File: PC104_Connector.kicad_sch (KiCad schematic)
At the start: 2 parts

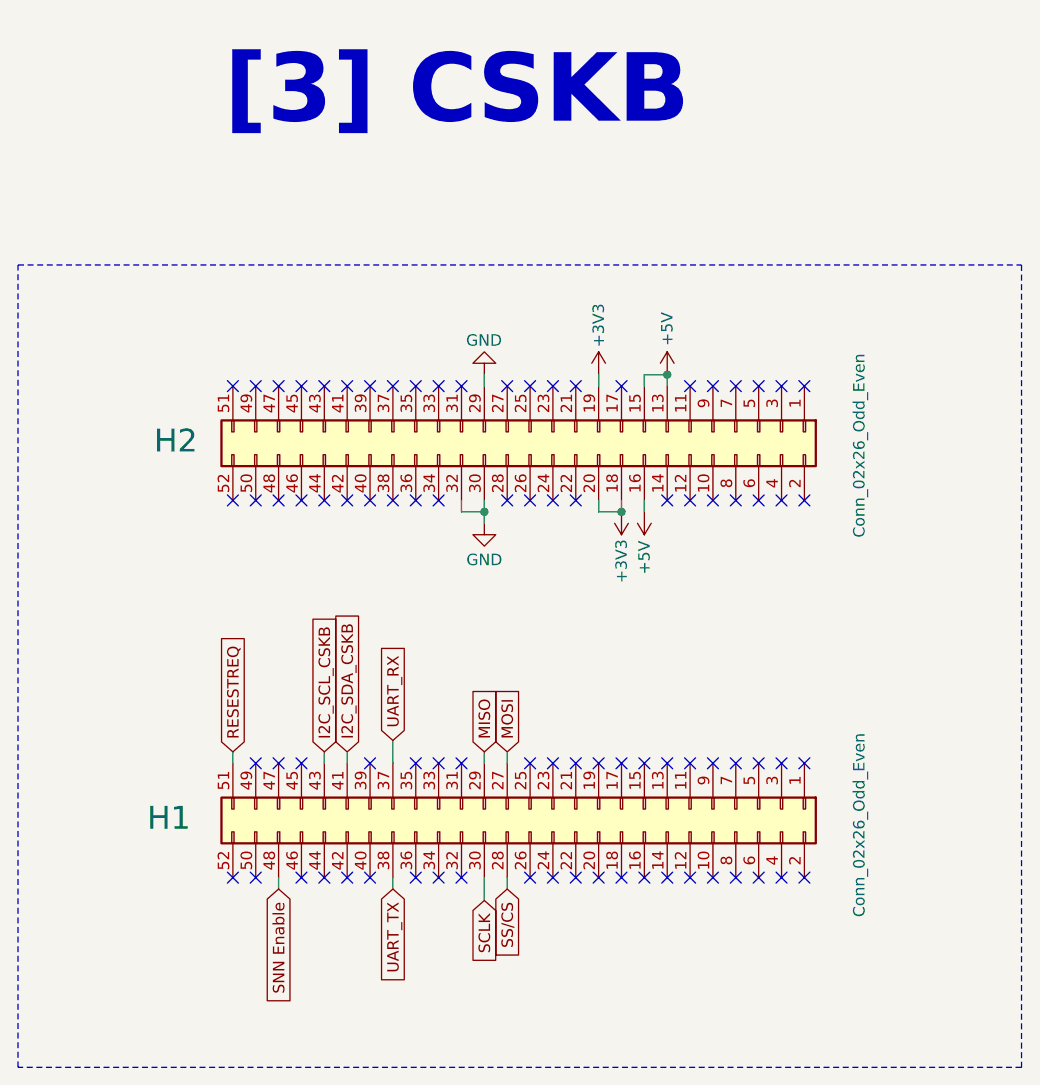
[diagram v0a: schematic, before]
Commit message: BOM update
completed the BOM list
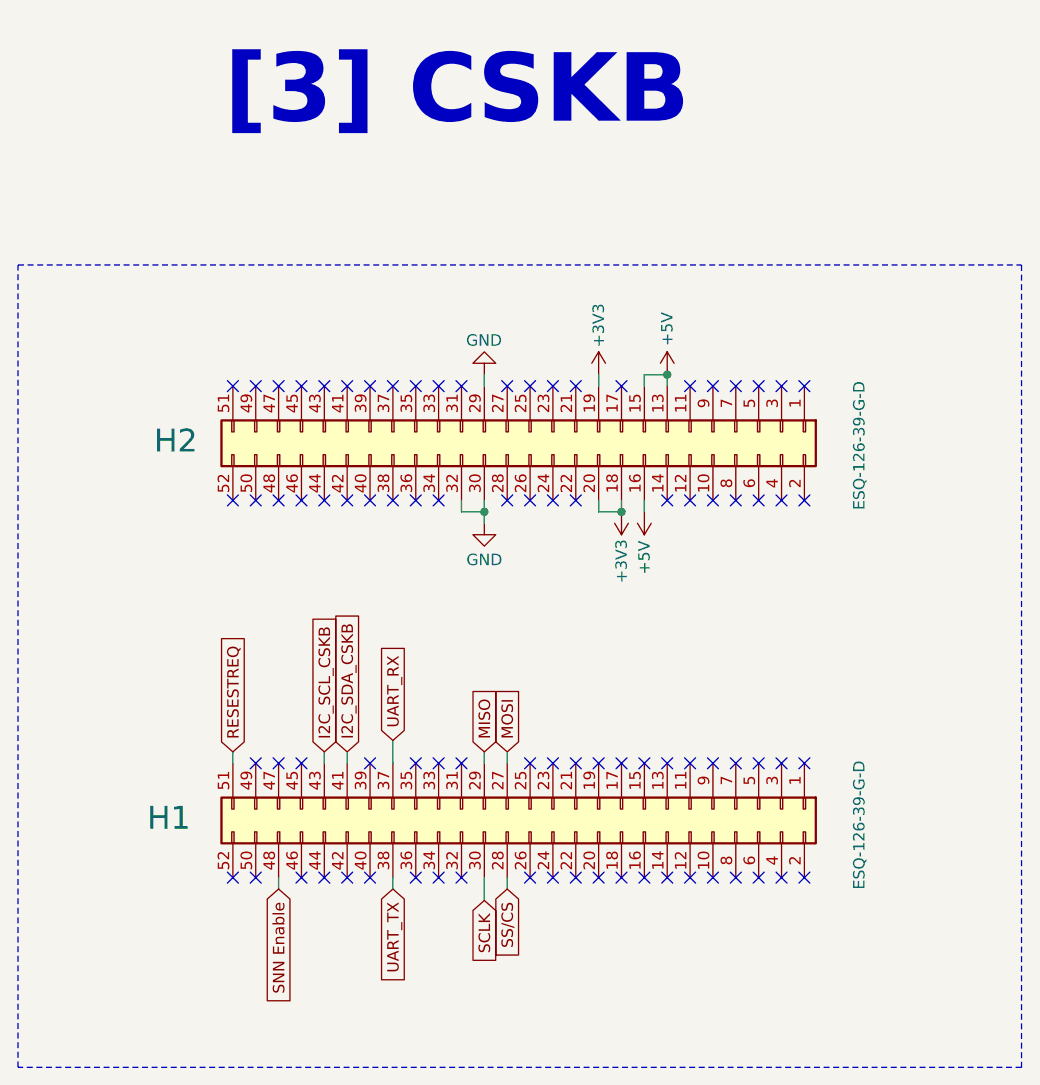
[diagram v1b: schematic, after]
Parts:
- H1, H2: value Conn_02x26_Odd_Even -> ESQ-126-39-G-D; MANUFACTURER (none) -> SAMTEC; MANUFACTURER_PART_NUMBER (none) -> ESQ-126-39-G-D
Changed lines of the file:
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@@
 			)
 		)
-		(property "Value" "Conn_02x26_Odd_Even"
+		(property "Value" "ESQ-126-39-G-D"
 			(at 188.976 107.188 0)
 			(effects
@@
 		(property "Description" "Generic connector, double row, 02x26, odd/even pin numbering scheme (row 1 odd numbers, row 2 even numbers), script generated (kicad-library-utils/schlib/autogen/connector/)"
 			(at 152.4 105.41 0)
+			(effects
+				(font
+					(size 1.27 1.27)
+				)
+				(hide yes)
+			)
+		)
+		(property "MANUFACTURER" "SAMTEC"
+			(at 152.4 105.41 90)
+			(effects
+				(font
+					(size 1.27 1.27)
+				)
+				(hide yes)
+			)
+		)
+		(property "MANUFACTURER_PART_NUMBER" "ESQ-126-39-G-D"
+			(at 152.4 105.41 90)
 			(effects
 				(font
@@
 			)
 		)
-		(property "Value" "Conn_02x26_Odd_Even"
+		(property "Value" "ESQ-126-39-G-D"
 			(at 188.976 65.024 0)
 			(effects
@@
 			(effects
 				(font
+					(size 1.27 1.27)
+				)
+				(hide yes)
+			)
+		)
+		(property "MANUFACTURER" "SAMTEC"
+			(at 152.4 63.5 90)
+			(effects
+				(font
+					(size 1.27 1.27)
+				)
+				(hide yes)
+			)
+		)
+		(property "MANUFACTURER_PART_NUMBER" "ESQ-126-39-G-D"
+			(at 152.4 63.5 90)
+			(effects
+				(font
